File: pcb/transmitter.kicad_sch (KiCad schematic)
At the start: 39 parts, among them J1 Conn_Coaxial, SW1 SW_DIP_x04, U2 STM32WL55CCUx, Y1 Crystal_GND23, Y2 Crystal

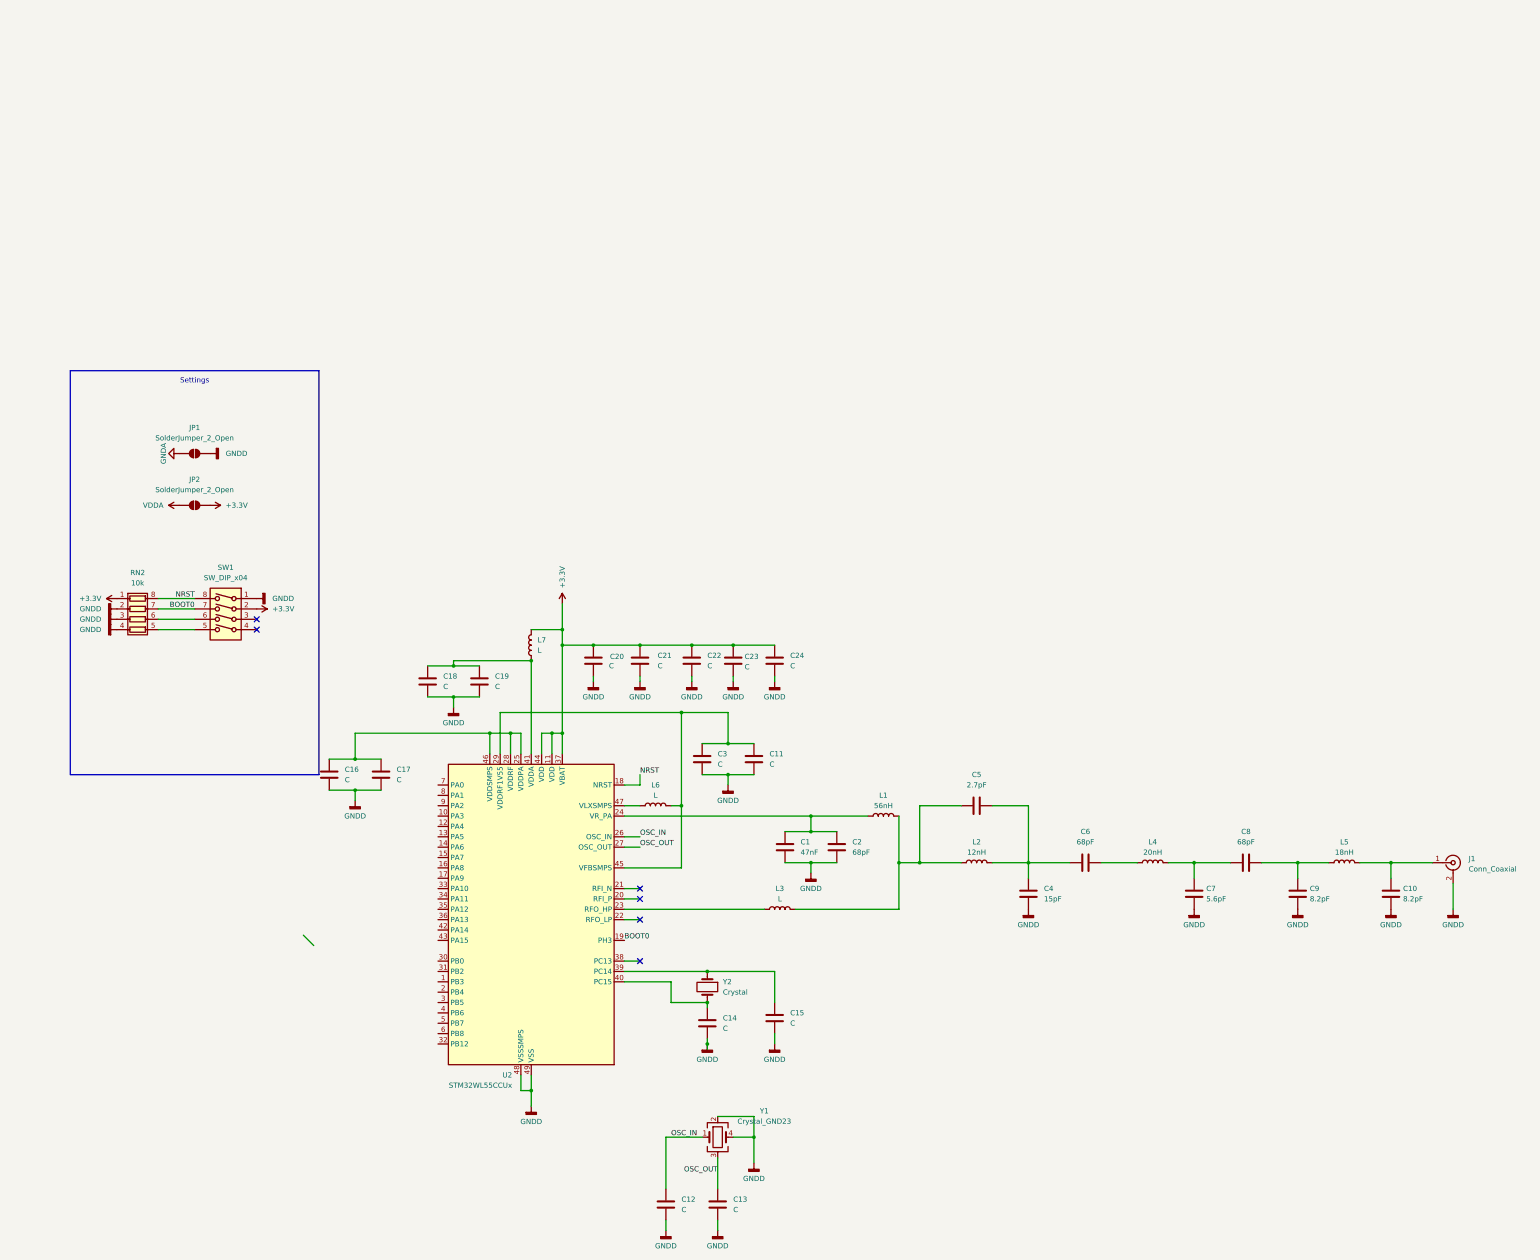
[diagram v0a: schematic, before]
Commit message: Updated schematics and removed most test points
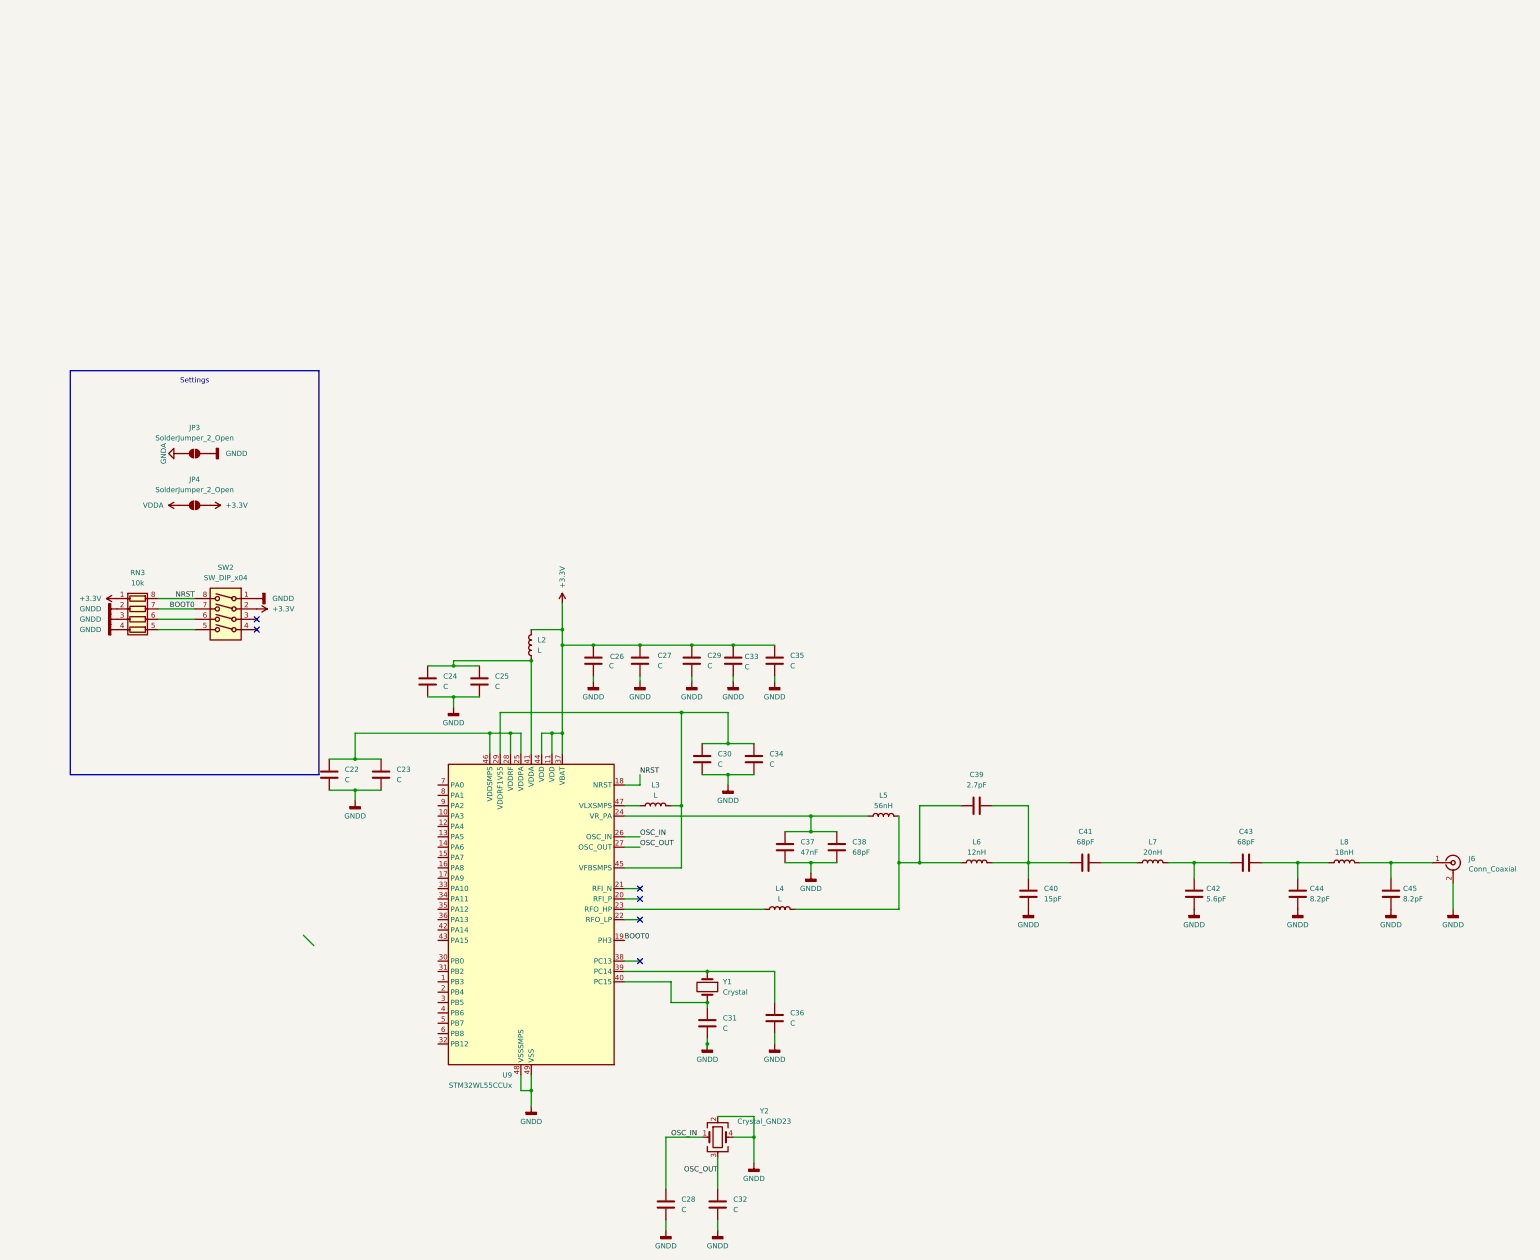
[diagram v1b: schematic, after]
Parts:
- removed JP1, JP2: SolderJumper_2_Open, Jumper:SolderJumper-2_P1.3mm_Open_RoundedPad1.0x1.5mm, symbol Jumper:SolderJumper_2_Open
- removed RN2: 10k, Resistor_SMD:R_Array_Convex_4x0612, symbol Device:R_Pack04
- removed SW1: SW_DIP_x04, Button_Switch_SMD:SW_DIP_SPSTx04_Slide_Copal_CHS-04A_W5.08mm_P1.27mm_JPin, symbol Switch:SW_DIP_x04
- added JP3, JP4: SolderJumper_2_Open, Jumper:SolderJumper-2_P1.3mm_Open_RoundedPad1.0x1.5mm, symbol Jumper:SolderJumper_2_Open
- added RN3: 10k, Resistor_SMD:R_Array_Convex_4x0612, symbol Device:R_Pack04
- added SW2: SW_DIP_x04, Button_Switch_SMD:SW_DIP_SPSTx04_Slide_Copal_CHS-04A_W5.08mm_P1.27mm_JPin, symbol Switch:SW_DIP_x04
- renumbered C16 to C22, C17 to C23, C18 to C24, C19 to C25, C20 to C26, C21 to C27, C12 to C28, C22 to C29, C3 to C30, C14 to C31, C13 to C32, C23 to C33, C11 to C34, C24 to C35, C15 to C36, C1 to C37, C2 to C38, C5 to C39, C4 to C40, C6 to C41, C7 to C42, C8 to C43, C9 to C44, C10 to C45, J1 to J6, L7 to L2, L6 to L3, L3 to L4, L1 to L5, L2 to L6, L4 to L7, L5 to L8, U2 to U9, Y2 to Y1, Y1 to Y2
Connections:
- net +3.3V: now also JP4.1 (A), RN3.1 (R1.1), SW2.2
- net BOOT0: now also RN3.7 (R2.2), SW2.7
- net GNDA: now also JP3.2 (B)
- net GNDD: now also JP3.1 (A), RN3.2 (R2.1), RN3.3 (R3.1), RN3.4 (R4.1), SW2.1
- net NRST: now also RN3.8 (R1.2), SW2.8
- net VDDA: now also JP4.2 (B)
- new net: RN3.5 (R4.2), SW2.5
- new net: RN3.6 (R3.2), SW2.6
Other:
- company: (none) -> Rowan Rocketry
- title: (none) -> Control Module Rev2

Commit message: Updated PCB Layout and routing
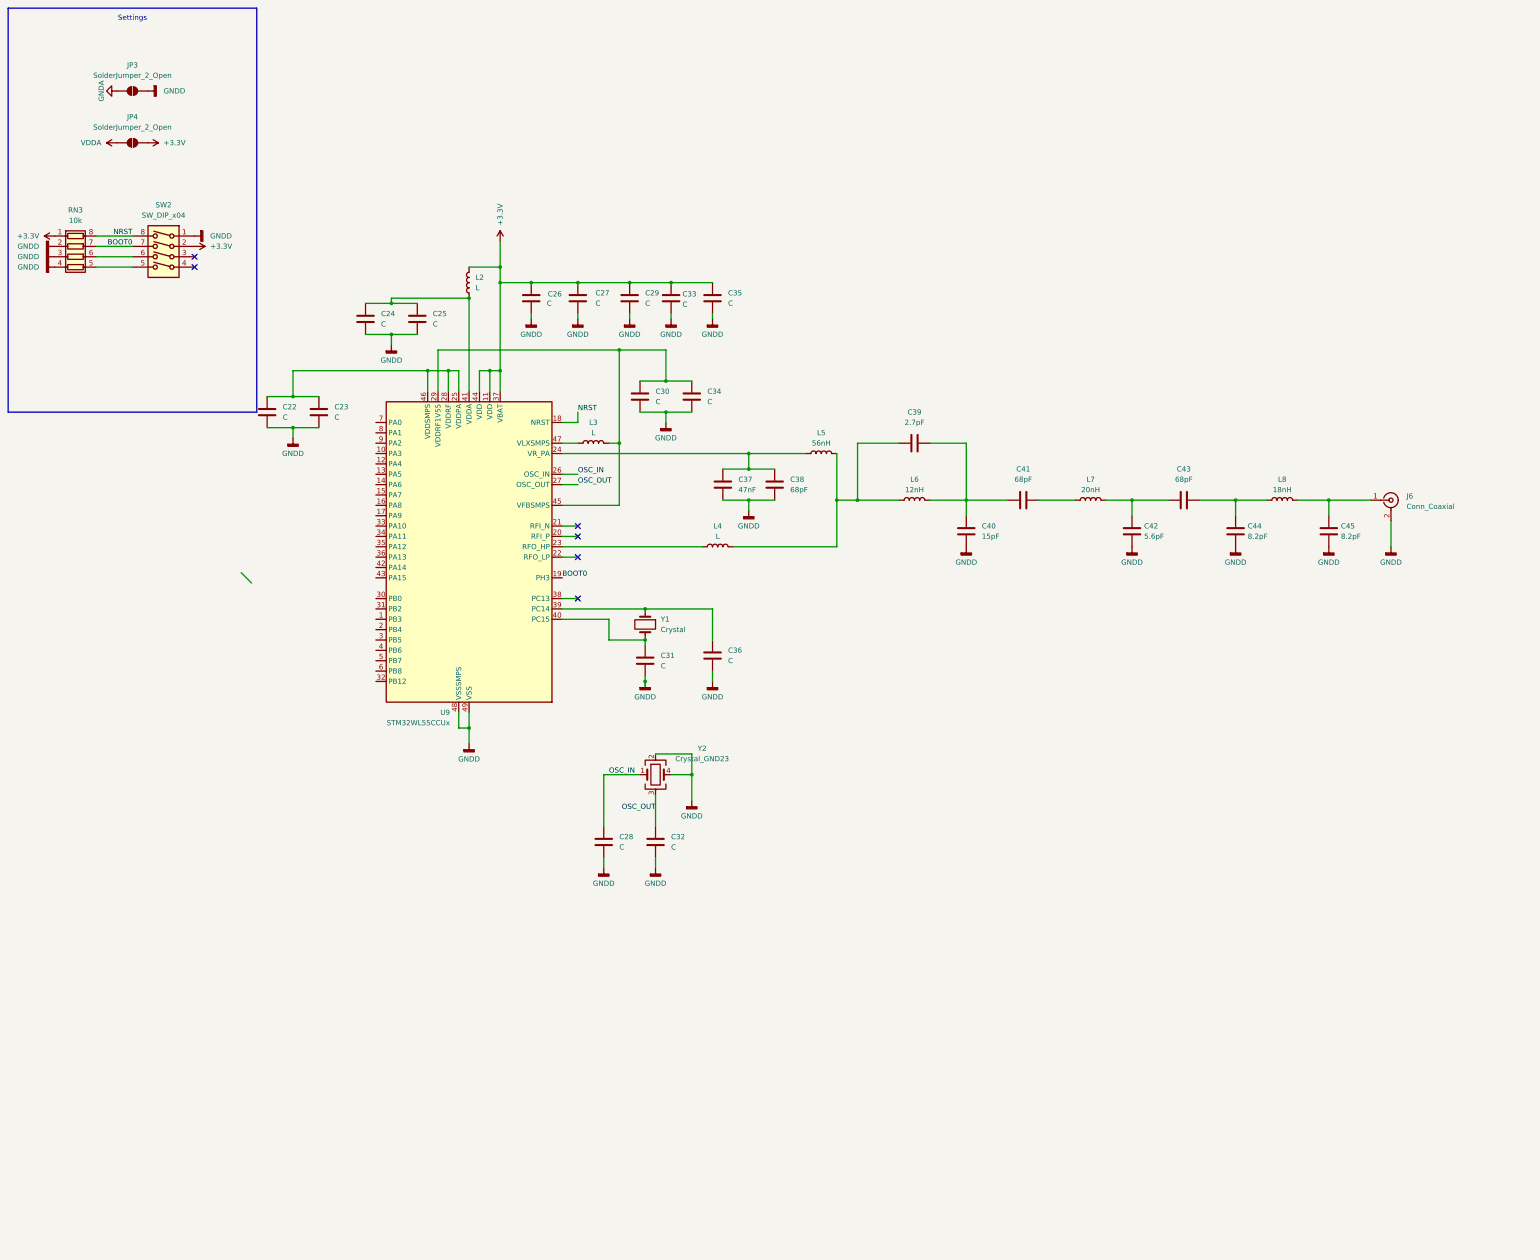
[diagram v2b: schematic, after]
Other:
- moved on the sheet: C22, C23, C24, C25, C26, C27, C28, C29, C30, C31, C32, C33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
